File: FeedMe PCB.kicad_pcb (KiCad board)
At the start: 2 copper layers, 70 x 40 mm, 29 parts, among them J1 Battery In (12V), J2 Solar Charger In, J3 E-Paper Display, J4 Seeed Studio Xiao ESP32-C6, J5 Motor Out, Q1 2N7002, Q2 AO3401A, U1 TPS562200

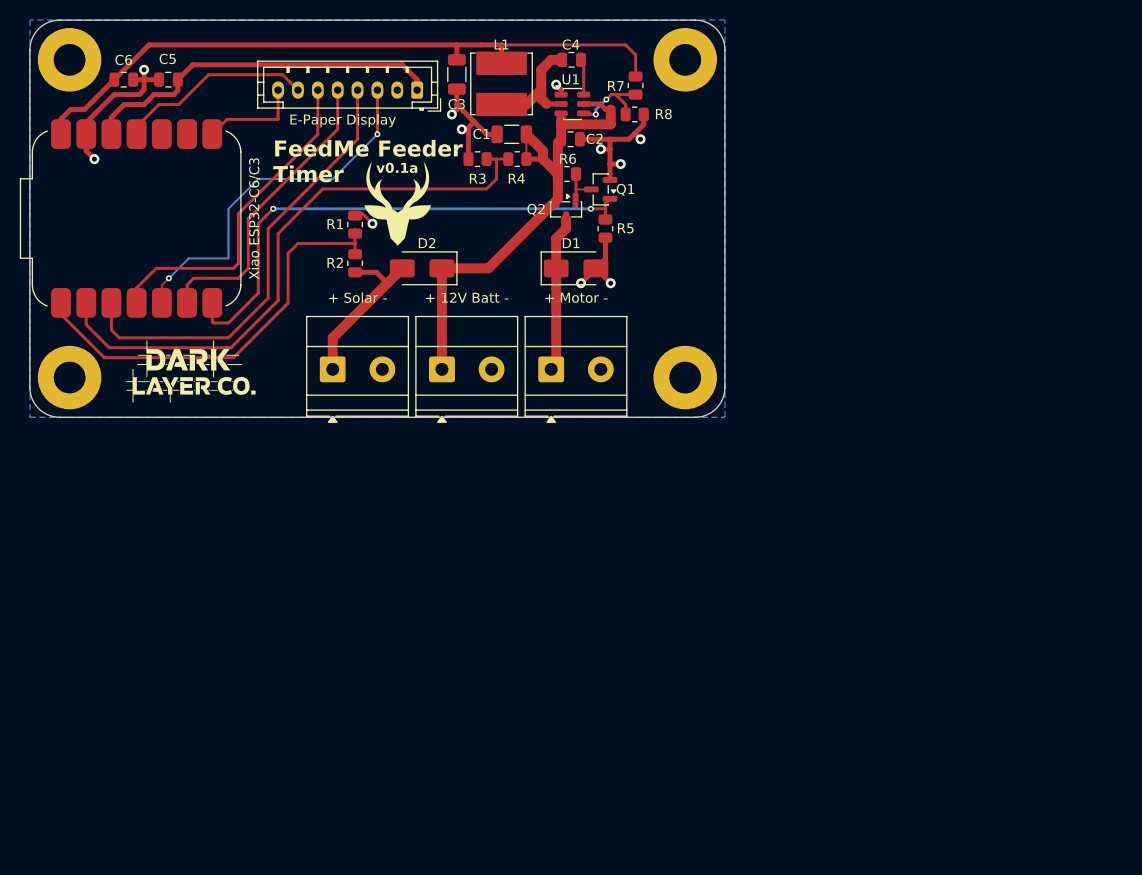
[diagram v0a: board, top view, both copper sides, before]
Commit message: v0.1b - Buck-boost converter, pluggable terminals, reliability fixes
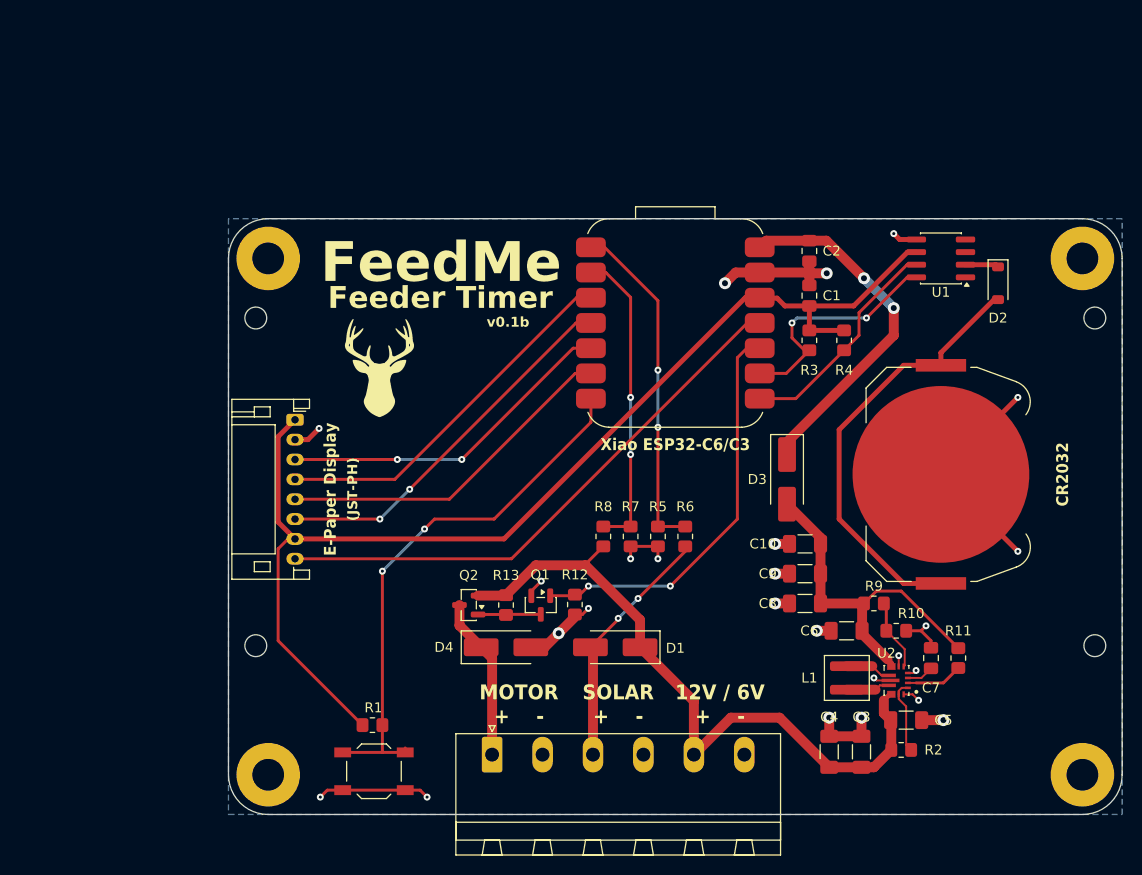
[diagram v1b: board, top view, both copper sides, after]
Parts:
- removed J4: Seeed Studio Xiao ESP32-C6, Footprints:MCU_Seeed_Xiao_ESP32C6
- removed J5: Motor Out, TerminalBlock_Phoenix:TerminalBlock_Phoenix_MKDS-1,5-2_1x02_P5.00mm_Horizontal
- removed the REF** at (146.0, 76.0)
- removed the REF** at (84.0, 44.0)
- removed the REF** at (84.0, 76.0)
- removed the REF** at (146.0, 44.0)
- added BT1: CR2032, Battery:BatteryHolder_Keystone_3034_1x20mm, F.Cu at (171.8, 85.8)
- added C10: 22uF, Capacitor_SMD:C_1206_3216Metric_Pad1.33x1.80mm_HandSolder, F.Cu at (158.1, 92.8)
- added C7: 100nF, Capacitor_SMD:C_0805_2012Metric_Pad1.18x1.45mm_HandSolder, F.Cu at (170.8, 104.2)
- added C8: 22uF, Capacitor_SMD:C_1206_3216Metric_Pad1.33x1.80mm_HandSolder, F.Cu at (158.1, 98.8)
- added C9: 22uF, Capacitor_SMD:C_1206_3216Metric_Pad1.33x1.80mm_HandSolder, F.Cu at (158.1, 95.8)
- added D3: SS14, Diode_SMD:D_SMA_Handsoldering, F.Cu at (156.2, 86.2)
- added D4: SS14, Diode_SMD:D_SMA_Handsoldering, F.Cu at (128.0, 103.2)
- added R10: 100K, Resistor_SMD:R_0805_2012Metric_Pad1.20x1.40mm_HandSolder, F.Cu at (167.2, 101.5)
- added R11: 100K, Resistor_SMD:R_0805_2012Metric_Pad1.20x1.40mm_HandSolder, F.Cu at (173.5, 104.2)
- added R12: 10K, Resistor_SMD:R_0805_2012Metric_Pad1.20x1.40mm_HandSolder, F.Cu at (134.9, 98.9)
- added R13: 10K, Resistor_SMD:R_0805_2012Metric_Pad1.20x1.40mm_HandSolder, F.Cu at (128.0, 98.9)
- added R9: 560K, Resistor_SMD:R_0805_2012Metric_Pad1.20x1.40mm_HandSolder, F.Cu at (165.0, 98.8)
- added REF**: MountingHole_3.2mm_M3_Pad, MountingHole:MountingHole_3.2mm_M3_Pad, F.Cu at (186.0, 64.0)
- added REF**: MountingHole_3.2mm_M3_Pad, MountingHole:MountingHole_3.2mm_M3_Pad, F.Cu at (104.0, 64.0)
- added REF**: MountingHole_3.2mm_M3_Pad, MountingHole:MountingHole_3.2mm_M3_Pad, F.Cu at (186.0, 116.0)
- added REF**: MountingHole_3.2mm_M3_Pad, MountingHole:MountingHole_3.2mm_M3_Pad, F.Cu at (104.0, 116.0)
- added REF**: Waveshare_2.9in_ePaper_Mounting, Footprints:Waveshare_2.9in_ePaper_Mounting, F.Cu at (102.8, 70.0)
- added SW1: SW_Push, Button_Switch_SMD:SW_SPST_TL3342, F.Cu at (114.7, 115.7)
- added U2: TPS63070RNMR, Footprints:VREG_TPS63070RNMR, F.Cu at (167.3, 106.5)
- C1: value 22uF -> 100nF; footprint Capacitor_SMD:C_1206_3216Metric -> Capacitor_SMD:C_0805_2012Metric_Pad1.18x1.45mm_HandSolder
- C2: value 100nF -> 10uF; footprint Capacitor_SMD:C_0805_2012Metric -> Capacitor_SMD:C_0805_2012Metric_Pad1.18x1.45mm_HandSolder
- C3: value 22uF -> 10uF; footprint Capacitor_SMD:C_1206_3216Metric -> Capacitor_SMD:C_1206_3216Metric_Pad1.33x1.80mm_HandSolder
- C4, C5: value 100nF -> 10uF; footprint Capacitor_SMD:C_0805_2012Metric -> Capacitor_SMD:C_1206_3216Metric_Pad1.33x1.80mm_HandSolder
- C6: footprint Capacitor_SMD:C_0805_2012Metric -> Capacitor_SMD:C_1206_3216Metric_Pad1.33x1.80mm_HandSolder
- D1: footprint Diode_SMD:D_SMA -> Diode_SMD:D_SMA_Handsoldering
- D2: value SS14 -> Schottky; footprint Diode_SMD:D_SMA -> Diode_SMD:D_SOD-123
- J1: value Battery In (12V) -> Screw_Terminal_01x06; footprint TerminalBlock_Phoenix:TerminalBlock_Phoenix_MKDS-1,5-2_1x02_P5.00mm_Horizontal -> Connector_Phoenix_MSTB:PhoenixContact_MSTBA_2,5_6-G-5,08_1x06_P5.08mm_Horizontal
- J2: value Solar Charger In -> Seeed Studio Xiao ESP32-C6/C3; footprint TerminalBlock_Phoenix:TerminalBlock_Phoenix_MKDS-1,5-2_1x02_P5.00mm_Horizontal -> Footprints:MCU_Seeed_Xiao_ESP32C6_Castellated
- J3: footprint Connector_JST:JST_PH_B8B-PH-K_1x08_P2.00mm_Vertical -> Connector_JST:JST_PH_S8B-PH-K_1x08_P2.00mm_Horizontal
- L1: value 10uH -> 1.5uH; footprint Inductor_SMD:L_Bourns_SRN6045TA -> Inductor_SMD:L_Coilcraft_XAL4030-XXX
- R1, R3: value 27K -> 4.7K; footprint Resistor_SMD:R_0805_2012Metric -> Resistor_SMD:R_0805_2012Metric_Pad1.20x1.40mm_HandSolder
- R2: value 100K -> 10K; footprint Resistor_SMD:R_0805_2012Metric -> Resistor_SMD:R_0805_2012Metric_Pad1.20x1.40mm_HandSolder
- R4: value 100K -> 4.7K; footprint Resistor_SMD:R_0805_2012Metric -> Resistor_SMD:R_0805_2012Metric_Pad1.20x1.40mm_HandSolder
- R5: value 10K -> 27K; footprint Resistor_SMD:R_0805_2012Metric -> Resistor_SMD:R_0805_2012Metric_Pad1.20x1.40mm_HandSolder
- R6, R8: value 10K -> 100K; footprint Resistor_SMD:R_0805_2012Metric -> Resistor_SMD:R_0805_2012Metric_Pad1.20x1.40mm_HandSolder
- R7: value 51K -> 27K; footprint Resistor_SMD:R_0805_2012Metric -> Resistor_SMD:R_0805_2012Metric_Pad1.20x1.40mm_HandSolder
- U1: value TPS562200 -> DS3231M; footprint Package_TO_SOT_SMD:SOT-23-6 -> Package_SO:SOIC-8_3.9x4.9mm_P1.27mm
- moved C5 98.4 mm to (168.2, 110.5), turned to 0 degrees
- moved C6 91.5 mm to (162.2, 101.5), turned to 180 degrees
- moved C3 79.5 mm to (163.8, 113.7)
- moved C4 74.4 mm to (160.5, 113.7), turned to 90 degrees
- moved R2 73.7 mm to (167.8, 113.5), turned to 180 degrees
- moved L1 69.2 mm to (162.3, 106.2), turned to 90 degrees
- moved D2 58.0 mm to (177.5, 66.5), turned to -90 degrees
- moved R1 50.4 mm to (114.5, 111.0), turned to 180 degrees
- moved R7 45.4 mm to (140.5, 92.0)
- moved R8 42.6 mm to (137.8, 92.0), turned to -90 degrees
- moved Q1 42.3 mm to (131.4, 98.9), turned to -90 degrees
- moved Q2 41.0 mm to (124.2, 98.9), turned to 180 degrees
- moved U1 40.2 mm to (171.8, 64.0), turned to 180 degrees
- moved J1 39.1 mm to (126.5, 114.0)
- moved R6 38.4 mm to (146.0, 92.0), turned to -90 degrees
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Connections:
- C1 pad 1: +12V -> +3V3
- C2 pad 1: +12V -> +5V
- C3 pad 1: GND -> +VIN
- C3 pad 2: +5V -> GND
- C4 pad 1: Net-(U1-SW) -> +VIN
- C4 pad 2: Net-(U1-VBST) -> GND
- C5 pad 1: +3V3 -> +VIN
- C6 pad 1: +5V -> Net-(D3-A)
- D1 pad 1: MOTOR+ -> +VIN
- D1 pad 2: GND -> SOLAR+
- D2 pad 1: +12V -> Net-(D2-K)
- D2 pad 2: SOLAR+ -> Net-(BT1-+)
- J1 pad 1: +12V -> MOTOR+
- J2 pad 1: SOLAR+ -> SOLAR_SENSE
- J2 pad 2: GND -> BATT_SENSE
- J3 pad 7: EPD_RST -> +3V3
- L1 pad 1: +5V -> Net-(U2-L1)
- L1 pad 2: Net-(U1-SW) -> Net-(U2-L2)
- Q2 pad 2: +12V -> +VIN
- R1 pad 1: GND -> BTN1
- R1 pad 2: SOLAR_SENSE -> +3V3
- R2 pad 1: SOLAR_SENSE -> Net-(U2-EN)
- R2 pad 2: SOLAR+ -> +VIN
- R3 pad 1: GND -> +3V3
- R3 pad 2: BATT_SENSE -> I2C_SCL
- R4 pad 1: BATT_SENSE -> I2C_SDA
- R4 pad 2: +12V -> +3V3
- R5 pad 1: MOTOR_CTRL -> GND
- R5 pad 2: GND -> SOLAR_SENSE
- R6 pad 1: Net-(Q1-D) -> SOLAR_SENSE
- R6 pad 2: +12V -> SOLAR+
- R7 pad 1: Net-(U1-VFB) -> GND
- R7 pad 2: +5V -> BATT_SENSE
- R8 pad 1: Net-(U1-VFB) -> BATT_SENSE
- R8 pad 2: GND -> +VIN
- U1 pad 1: GND -> unconnected-(U1-32KHZ-Pad1)
- U1 pad 2: Net-(U1-SW) -> Net-(D2-K)
- U1 pad 3: +12V -> unconnected-(U1-~{INT}/SQW-Pad3)
- U1 pad 4: Net-(U1-VFB) -> unconnected-(U1-~{RST}-Pad4)
- U1 pad 5: +12V -> GND
- U1 pad 6: Net-(U1-VBST) -> +3V3
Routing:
- net +3V3: track 38.2 -> 118.0 mm
- net +VIN: track 0.00 -> 68.8 mm
- net BTN1: track 0.00 -> 54.6 mm, vias 0 -> 2
- net +12V: track 52.4 -> 0.00 mm
- net EPD_BUSY: track 10.2 -> 56.6 mm
- net Net-(BT1-+): track 0.00 -> 44.1 mm
- net GND: track 55.2 -> 91.3 mm, vias 11 -> 25
- net Net-(D3-A): track 0.00 -> 35.8 mm
- net +5V: track 68.4 -> 35.8 mm, vias 0 -> 2
- net BATT_SENSE: track 59.7 -> 30.9 mm, vias 0 -> 2
- net I2C_SCL: track 0.00 -> 24.2 mm, vias 0 -> 2
- net I2C_SDA: track 0.00 -> 22.9 mm
- net EPD_RST: track 21.1 -> 0.00 mm
- net Net-(U1-SW): track 12.3 -> 0.00 mm
- net MOTOR_CTRL: track 52.7 -> 40.9 mm
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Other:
- board size 70 x 40 mm -> 90 x 60 mm
- board text added: "- +"
- board text added: "12V / 6V + -"
- board text added: "BATTERY"
- board text added: "DarkLayer.co"
- board text added: "FeedMe"
- board text added: "Feeder Timer"
- board text added: "MOTOR"
- board text added: "MOTOR + -"
- board text added: "SOLAR"
- board text added: "SOLAR + -"
- board text added: "v0.1b"
- board text removed: "FeedMe Feeder Timer"
- board text removed: "v0.1a"
